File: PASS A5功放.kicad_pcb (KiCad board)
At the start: 6 copper layers, 200 x 100 mm, 109 parts, among them IC1 OPA1611AIDR, IC2 LM317AEMPX_NOPB, IC3 LM337IMP_NOPB, Q1 IRF9610PBF, Q11 BCP56-16,115, Q12 BCP56-16,115, Q2 IRF9610PBF, Q3 IRF9610PBF, Q4 IRFP240PBF, Q5 IRFP240PBF, Q6 IRFP240PBF, Q7 IRFP240PBF, Q8 IRFP240PBF, Q9 IRFP240PBF, U1 UPC1237HA, U2 SFH6206-2T

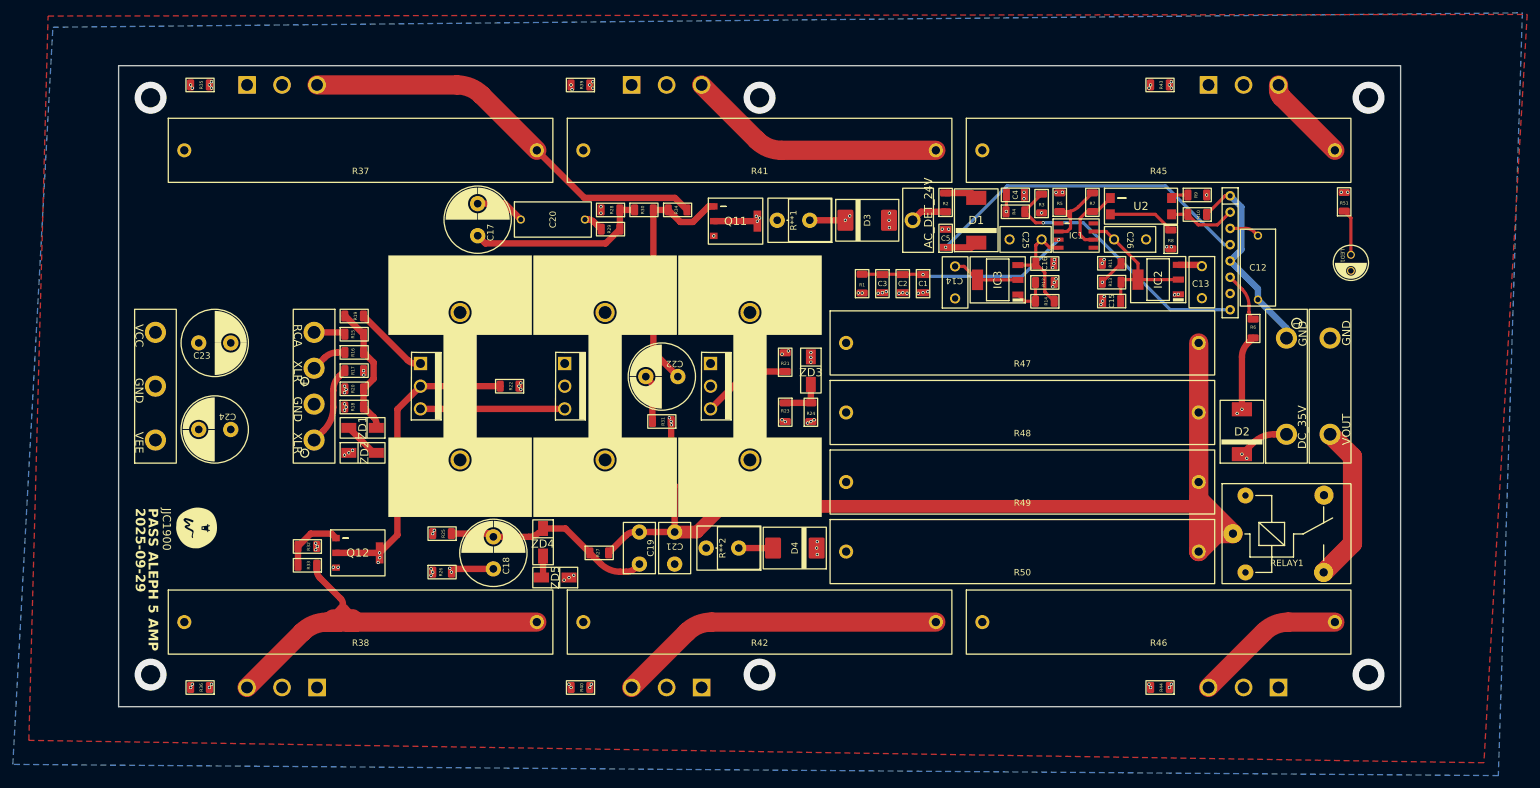
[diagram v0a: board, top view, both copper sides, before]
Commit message: using SMD power resistor
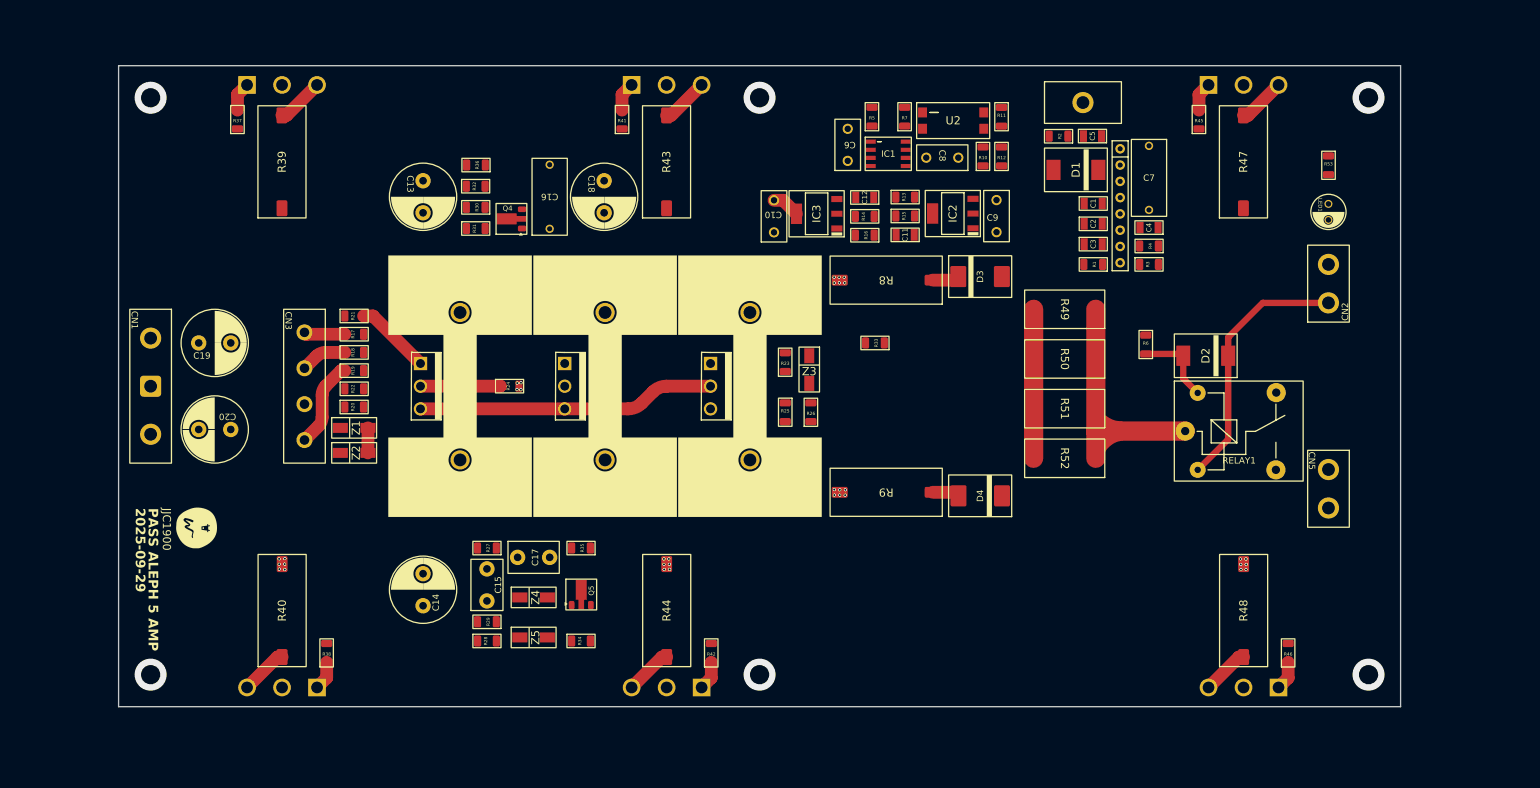
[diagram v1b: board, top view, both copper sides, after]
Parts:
- removed ZD1, ZD2, ZD3, ZD4, ZD5: SMAZ9V1-13-F, cus_zener:SMAZ9V1-13-F
- added Z1: SMAZ9V1-13-F, cus_zener:SMAZ9V1-13-F, F.Cu at (151.8, 161.5)
- added Z2: SMAZ9V1-13-F, cus_zener:SMAZ9V1-13-F, F.Cu at (151.8, 165.4)
- added Z3: SMAZ9V1-13-F, cus_zener:SMAZ9V1-13-F, F.Cu at (222.8, 152.4)
- added Z4: SMAZ9V1-13-F, cus_zener:SMAZ9V1-13-F, F.Cu at (179.8, 187.9)
- added Z5: SMAZ9V1-13-F, cus_zener:SMAZ9V1-13-F, F.Cu at (179.8, 194.2)
- CN1: footprint connectors:4线焊盘 -> connectors:3线焊盘
- CN4: footprint connectors:2线焊盘 -> connectors:1线焊盘
- Q10: renamed from Q8; footprint 3rd package:IRFP240PBF -> cus_mosfet:IRFP240PBF
- Q11: renamed from Q9; footprint 3rd package:IRFP240PBF -> cus_mosfet:IRFP240PBF
- Q4: renamed from Q11; footprint cus_transistor:BCP56-16,115 -> cus_transistor:BCX56-16,115
- Q5: renamed from Q12; footprint cus_transistor:BCP56-16,115 -> cus_transistor:BCX56-16,115
- Q6: renamed from Q4; footprint 3rd package:IRFP240PBF -> cus_mosfet:IRFP240PBF
- Q7: renamed from Q5; footprint 3rd package:IRFP240PBF -> cus_mosfet:IRFP240PBF
- Q8: renamed from Q6; footprint 3rd package:IRFP240PBF -> cus_mosfet:IRFP240PBF
- Q9: renamed from Q7; footprint 3rd package:IRFP240PBF -> cus_mosfet:IRFP240PBF
- R10: renamed from R8; value 500 -> 487
- R17: renamed from R15; value 1kΩ -> 1k
- R21: renamed from R19; value 220Ω -> 220
- R25: renamed from R23; value 220Ω -> 220
- R27: renamed from R25; value 220Ω -> 220
- R35: renamed from R33; value 220Ω -> 220
- R39: renamed from R37; footprint generic package:R 10W -> cus_resistor:SMW51R0JT
- R40: renamed from R38; footprint generic package:R 10W -> cus_resistor:SMW51R0JT
- R43: renamed from R41; footprint generic package:R 10W -> cus_resistor:SMW51R0JT
- R44: renamed from R42; footprint generic package:R 10W -> cus_resistor:SMW51R0JT
- R47: renamed from R45; footprint generic package:R 10W -> cus_resistor:SMW51R0JT
- R48: renamed from R46; footprint generic package:R 10W -> cus_resistor:SMW51R0JT
- R49: renamed from R47; footprint generic package:R 10W -> cus_resistor:SMW3R47JT
- R50: renamed from R48; footprint generic package:R 10W -> cus_resistor:SMW3R47JT
- R51: renamed from R49; footprint generic package:R 10W -> cus_resistor:SMW3R47JT
- R52: renamed from R50; footprint generic package:R 10W -> cus_resistor:SMW3R47JT
- R8: renamed from R**1; footprint cus_resistor:RSF5SSJT-73-150R_Vertical -> cus_resistor:SMW 5W 150R J
- R9: renamed from R**2; footprint cus_resistor:RSF5SSJT-73-150R_Vertical -> cus_resistor:SMW 5W 150R J
- moved R34 45.2 mm to (187.1, 194.8), turned to 0 degrees
- moved R35 42.8 mm to (187.1, 180.2)
- moved R48 40.8 mm to (290.5, 190.0), turned to 90 degrees
- moved R47 40.8 mm to (290.5, 120.0), turned to 90 degrees
- moved R52 37.1 mm to (262.6, 166.2), turned to 180 degrees
- moved R1 36.2 mm to (267.1, 136.0), turned to 180 degrees
- moved R51 36.0 mm to (262.6, 158.5), turned to 180 degrees
- moved Q5 35.8 mm to (187.5, 187.5)
- moved R33 35.4 mm to (233.0, 148.2)
- moved R50 35.1 mm to (262.6, 150.8), turned to 180 degrees
- moved Q4 35.0 mm to (176.3, 128.6), turned to 90 degrees
- moved R49 34.5 mm to (262.6, 143.0), turned to 180 degrees
- moved C11 33.8 mm to (237.7, 131.4)
- moved R13 33.8 mm to (237.7, 125.5)
- moved R15 33.8 mm to (237.7, 128.4)
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- renumbered C14 to C10, C15 to C11, C16 to C12, C17 to C13, C18 to C14, C19 to C15, C20 to C16, C21 to C17, C22 to C18, C23 to C19, C24 to C20, C25 to C6, C12 to C7, C26 to C8, C13 to C9, R9 to R11, R10 to R12, R11 to R13, R12 to R14, R13 to R15, R14 to R16, R16 to R18, R17 to R19, R18 to R20, R20 to R22, R21 to R23, R22 to R24, R24 to R26, R26 to R28, R27 to R29, R28 to R30, R29 to R31, R30 to R32, R31 to R33, R32 to R34, R34 to R36, R35 to R37, R36 to R38, R39 to R41, R40 to R42, R43 to R45, R44 to R46, R51 to R53
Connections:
- C13 pad 1: Net-(C17-Pad1) -> Net-(C13-Pad1)
- C14 pad 1: Net-(C18-Pad1) -> Net-(C14-Pad1)
- C14 pad 2: Net-(ZD4-K) -> Net-(Z4-K)
- C15 pad 1: Net-(ZD4-K) -> /VIN
- C15 pad 2: /VIN -> Net-(Z4-K)
- C16 pad 1: Net-(LED1-K) -> Net-(Q4-C)
- C16 pad 2: Net-(Q11-C) -> Net-(LED1-K)
- C17 pad 1: Net-(Q1-D) -> /VIN
- C17 pad 2: /VIN -> Net-(Q1-D)
- C18 pad 2: Net-(C22-Pad2) -> Net-(C18-Pad2)
- Q10 pad 1: Net-(Q8-G) -> Net-(Q10-G)
- Q11 pad 3: Net-(Q9-S) -> Net-(Q11-S)
- Q4 pad 2: Net-(Q11-C) -> Net-(Q4-C)
- Q5 pad 1: Net-(Q12-B) -> Net-(Q5-B)
- Q6 pad 1: Net-(Q4-G) -> Net-(Q6-G)
- Q7 pad 3: Net-(Q5-S) -> Net-(Q7-S)
- Q8 pad 1: Net-(Q6-G) -> Net-(Q8-G)
- Q9 pad 3: Net-(Q7-S) -> Net-(Q9-S)
- R17 pad 2: Net-(ZD1-K) -> Net-(Z1-K)
- R18 pad 2: Net-(ZD1-K) -> Net-(Z1-K)
- R19 pad 2: Net-(C18-Pad1) -> Net-(C14-Pad1)
- R20 pad 1: GND -> Net-(Z1-K)
- R20 pad 2: Net-(ZD1-K) -> GND
- R21 pad 1: Net-(Q1-G) -> Net-(Z1-K)
- R21 pad 2: Net-(ZD1-K) -> Net-(Q1-G)
- R22 pad 1: GND -> Net-(Z1-K)
- R22 pad 2: Net-(ZD1-K) -> GND
- R24 pad 1: /VEE -> Net-(Q1-D)
- R24 pad 2: Net-(Q1-D) -> /VEE
- R25 pad 1: Net-(ZD3-A) -> Net-(Q2-G)
- R25 pad 2: Net-(Q2-G) -> Net-(Z3-A)
- R26 pad 1: GND -> Net-(Z3-A)
- R26 pad 2: Net-(ZD3-A) -> GND
- R27 pad 1: Net-(ZD4-K) -> Net-(Q3-G)
- R27 pad 2: Net-(Q3-G) -> Net-(Z4-K)
- R28 pad 1: GND -> Net-(C14-Pad1)
- R28 pad 2: Net-(C18-Pad1) -> GND
- R29 pad 1: Net-(ZD4-K) -> Net-(Z4-K)
- R30 pad 1: Net-(C17-Pad1) -> /VCC
- R30 pad 2: /VCC -> Net-(C13-Pad1)
- R31 pad 1: Net-(Q11-C) -> Net-(C13-Pad1)
- R31 pad 2: Net-(C17-Pad1) -> Net-(Q4-C)
- R32 pad 1: Net-(C17-Pad1) -> Net-(C13-Pad1)
- R33 pad 1: /VIN -> Net-(C18-Pad2)
- R33 pad 2: Net-(C22-Pad2) -> /VIN
- R34 pad 1: /VEE -> Net-(Q5-B)
- R34 pad 2: Net-(Q12-B) -> /VEE
- R35 pad 1: Net-(Q5-S) -> Net-(Q5-B)
- R35 pad 2: Net-(Q12-B) -> Net-(Q7-S)
- R37 pad 1: Net-(Q4-G) -> Net-(Q4-C)
- R37 pad 2: Net-(Q11-C) -> Net-(Q6-G)
- R40 pad 1: /VEE -> Net-(Q7-S)
- R40 pad 2: Net-(Q5-S) -> /VEE
- R41 pad 1: Net-(Q6-G) -> Net-(Q4-C)
- R41 pad 2: Net-(Q11-C) -> Net-(Q8-G)
- R44 pad 1: /VEE -> Net-(Q9-S)
- R44 pad 2: Net-(Q7-S) -> /VEE
- R45 pad 1: Net-(Q8-G) -> Net-(Q4-C)
- R45 pad 2: Net-(Q11-C) -> Net-(Q10-G)
- R48 pad 1: /VEE -> Net-(Q11-S)
- R48 pad 2: Net-(Q9-S) -> /VEE
- R49 pad 1: Net-(LED1-K) -> /VIN
- R49 pad 2: /VIN -> Net-(LED1-K)
- R50 pad 1: Net-(LED1-K) -> /VIN
- R50 pad 2: /VIN -> Net-(LED1-K)
- R51 pad 1: Net-(LED1-K) -> /VIN
- R51 pad 2: /VIN -> Net-(LED1-K)
- R52 pad 1: Net-(LED1-K) -> /VIN
- R52 pad 2: /VIN -> Net-(LED1-K)
- R53 pad 1: Net-(LED1-A) -> /VCC
- R53 pad 2: /VCC -> Net-(LED1-A)
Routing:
- net Net-(LED1-K): track 597.6 -> 23.2 mm, vias 1 -> 0
- net /VIN: track 208.3 -> 37.2 mm, vias 5 -> 0
- net GND1: track 84.2 -> 0.00 mm, vias 4 -> 0
- net Net-(Q1-D): track 86.4 -> 12.4 mm, vias 9 -> 0
- net Net-(Q5-S): track 69.5 -> 0.00 mm
- net /DC 35V: track 108.8 -> 40.5 mm, vias 4 -> 0
- net Net-(D3-K): track 69.6 -> 4.23 mm, vias 2 -> 0
- net Net-(D4-A): track 73.9 -> 8.62 mm
- net Net-(Q6-S): track 65.5 -> 7.44 mm
- net /UPC1237_PIN4: track 57.2 -> 0.00 mm, vias 1 -> 0
- net Net-(Q11-C): track 48.5 -> 0.00 mm, vias 9 -> 0
- net Net-(C18-Pad1): track 44.7 -> 0.00 mm, vias 4 -> 0
- net Net-(Q7-S): track 51.4 -> 7.44 mm
- net /UPC1237_PIN7: track 44.0 -> 0.00 mm, vias 1 -> 0
- net /UPC1237_PIN8: track 42.2 -> 0.00 mm, vias 1 -> 0
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- removed copper zone on F.Cu, net /VIN
- removed copper zone on In2.Cu, net /VIN
- removed copper zone on B.Cu, net GND
- removed copper zone on F.Cu, net GND
- removed copper zone on In1.Cu, net GND
- removed copper zone on In2.Cu, net GND
- removed copper zone on In3.Cu, net GND
- removed copper zone on In3.Cu, net Net-(Q1-D)
- removed copper zone on In2.Cu, net Net-(Q11-C)
